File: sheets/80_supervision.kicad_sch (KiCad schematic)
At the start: 0 parts

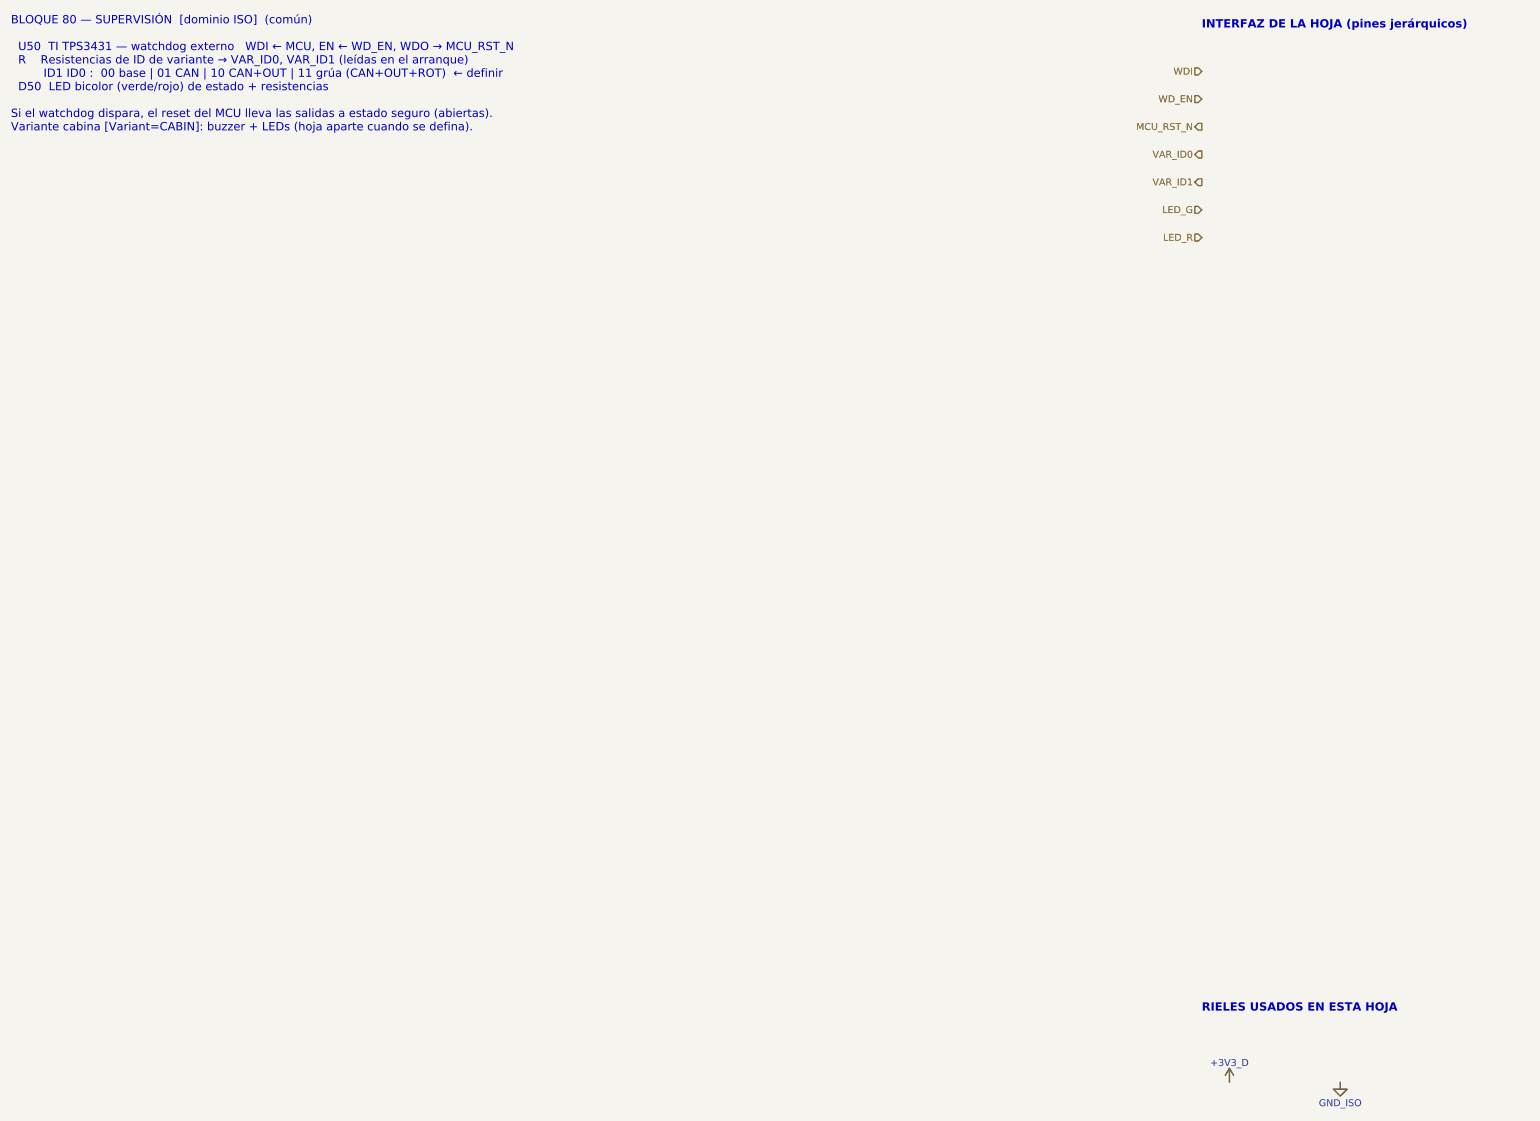
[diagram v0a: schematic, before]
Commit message: [Claude Code] 20_buck_5v: opción B (no aislada) con LMR38010; masas unificadas
- sheets/20_isolation -> sheets/20_buck_5v: se quitan PS201, ISO7763 y
  TPS7A1650; U201 LMR38010SQDDARQ1 (PROTO: LMR38010SDDAR, LCSC C5219310),
  5.02 V / 1 A a 400 kHz según TI SNVSC73B (L201 XAL6060-333, 3 x 22 uF,
  RT 64.9k, FB 100k/24.9k). Huella oficial HSOIC-8 con vías térmicas.
- Símbolo LMR38010 (easyeda2kicad) en lib/easyeda2kicad/INCLI-VA_easyeda,
  con tipos de pin ajustados; registrado en sym-lib-table.
- Todas las hojas: GND_ISO -> GND_VEH, +5V_ISO -> +5V_VEH.
- Raíz: EN/DIAG/FLT directos entre las hojas 40, 70 y 10; la hoja 20 sin pines.
- 10_power_input: R111 a +3V3_D, C109 = 100 nF (inrush con C105),
  C105 DNP solo en PROTO; se quita un PWR_FLAG suelto en GND_VEH.
- 70_output_ch: cambios de layout del usuario (hechos en KiCad).
- Textos de las hojas 30/40/50/80 y la raíz sin referencias al aislamiento.
- ERC: 0 en 10, 20, 30, 40, 50, 60 y 70; quedan los de 80 (hoja vacía).

Co-Authored-By: Claude Opus 5.5 <noreply@anthropic.com>
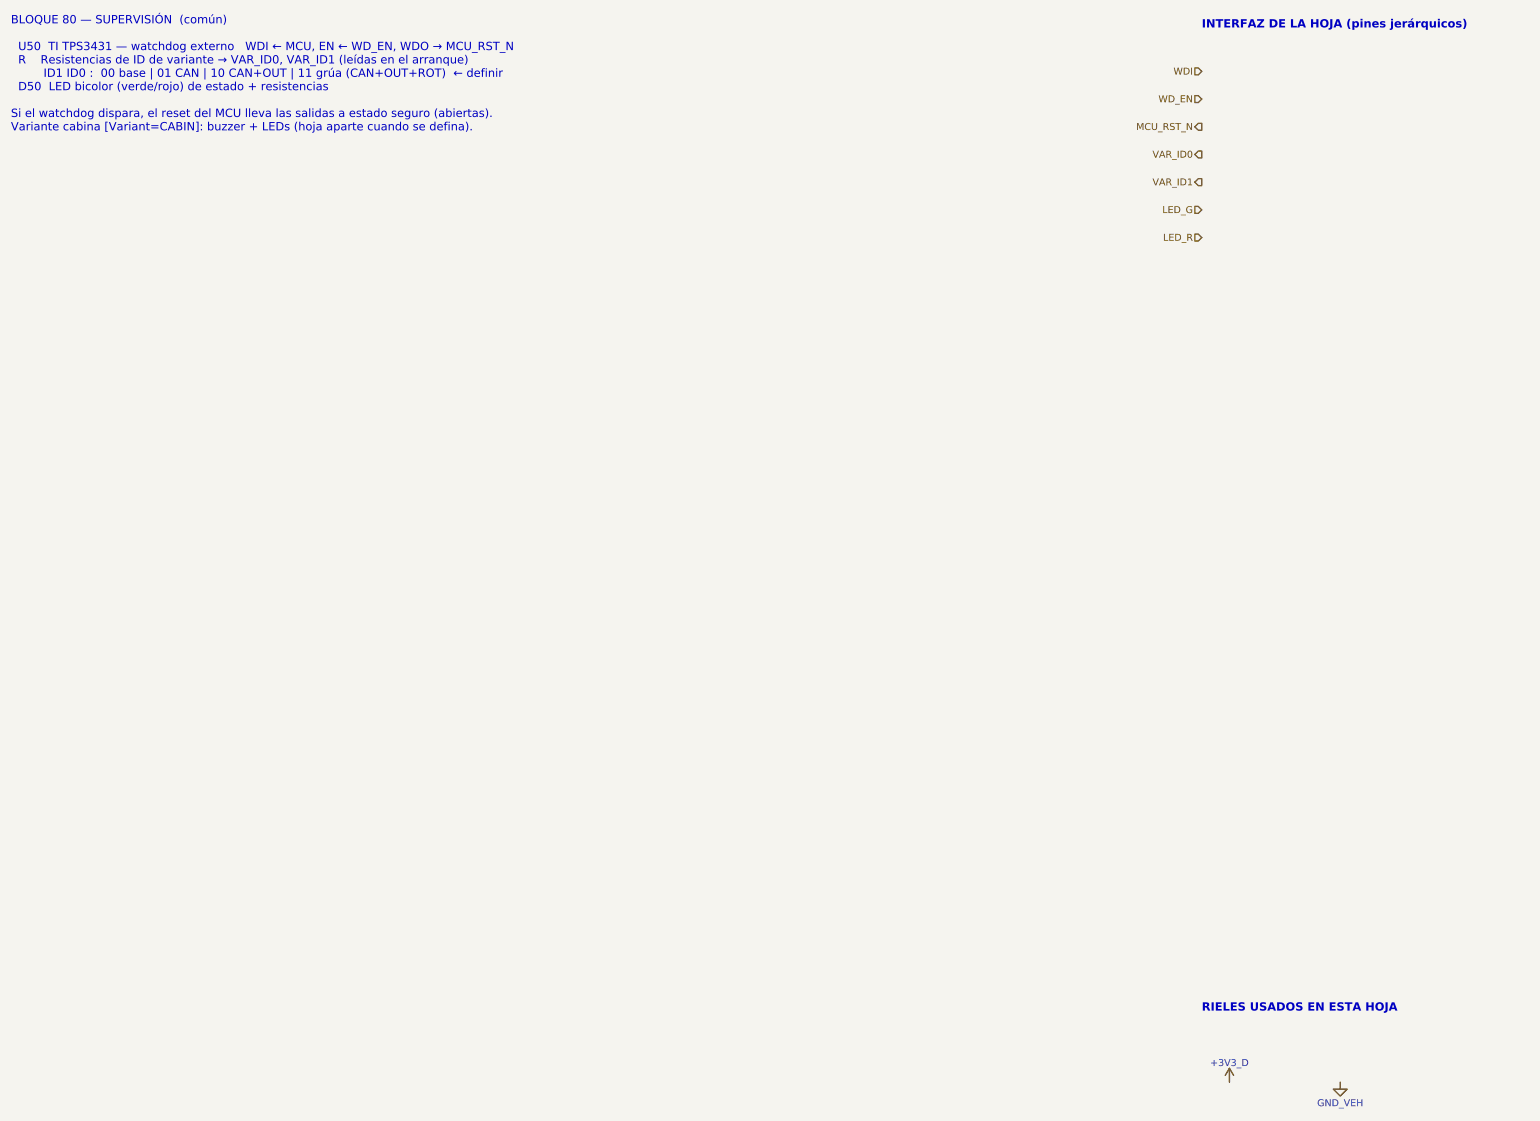
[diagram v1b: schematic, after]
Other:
- note added: "BLOQUE 80 — SUPERVISIÓN (común) U50 TI TPS3431 — watchdog externo WDI ← MCU, EN ← WD_EN, WDO → MCU_RST_N R Resistencias de ID de variante → VAR_ID0, VAR_ID1 (leídas en el arranque) ID1 ID0 : 00 base | 01 CAN | 10 CAN+OUT | 11 grúa (CAN+OUT+ROT) ← definir D50 LED bicolor (verde/rojo) de estado + resistencias Si el watchdog dispara, el reset del MCU lleva las salidas a estado seguro (abiertas). Var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"
- note removed: "BLOQUE 80 — SUPERVISIÓN [dominio ISO] (común) U50 TI TPS3431 — watchdog externo WDI ← MCU, EN ← WD_EN, WDO → MCU_RST_N R Resistencias de ID de variante → VAR_ID0, VAR_ID1 (leídas en el arranque) ID1 ID0 : 00 base | 01 CAN | 10 CAN+OUT | 11 grúa (CAN+OUT+ROT) ← definir D50 LED bicolor (verde/rojo) de estado + resistencias Si el watchdog dispara, el reset del MCU lleva las salidas a estado seguro (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"
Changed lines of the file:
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@@
 		(comment 2 "Inclinómetro de chasis CAN/BLE — INCLI-VA")
 	)
-	(text "BLOQUE 80 — SUPERVISIÓN  [dominio ISO]  (común)\n\n  U50  TI TPS3431 — watchdog externo   WDI ← MCU, EN ← WD_EN, WDO → MCU_RST_N\n  R    Resistencias de ID de variante → VAR_ID0, VAR_ID1 (leídas en el arranque)\n         ID1 ID0 :  00 base | 01 CAN | 10 CAN+OUT | 11 grúa (CAN+OUT+ROT)  ← definir\n  D50  LED bicolor (verde/rojo) de estado + resistencias\n\nSi el watchdog dispara, el reset del MCU lleva las salidas a estado seguro (abiertas).\nVariante cabina [Variant=CABIN]: buzzer + LEDs (hoja aparte cuando se defina)."
+	(text "BLOQUE 80 — SUPERVISIÓN  (común)\n\n  U50  TI TPS3431 — watchdog externo   WDI ← MCU, EN ← WD_EN, WDO → MCU_RST_N\n  R    Resistencias de ID de variante → VAR_ID0, VAR_ID1 (leídas en el arranque)\n         ID1 ID0 :  00 base | 01 CAN | 10 CAN+OUT | 11 grúa (CAN+OUT+ROT)  ← definir\n  D50  LED bicolor (verde/rojo) de estado + resistencias\n\nSi el watchdog dispara, el reset del MCU lleva las salidas a estado seguro (abiertas).\nVariante cabina [Variant=CABIN]: buzzer + LEDs (hoja aparte cuando se defina)."
 		(exclude_from_sim no)
 		(at 20.32 20.32 0)
@@
 	)
 	(symbol
-		(lib_id "INCLI-VA:GND_ISO")
+		(lib_id "INCLI-VA:GND_VEH")
 		(at 264.16 215.9 0)
 		(unit 1)
@@
 			)
 		)
-		(property "Value" "GND_ISO"
+		(property "Value" "GND_VEH"
 			(at 264.16 219.71 0)
 			(show_name no)

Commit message: [Claude Code] 80_supervision: TPS3828-33-Q1, LED y VAR_ID; J1/J2 verticales; contorno con muesca
- 80_supervision: U801 TPS3828-33QDBVRQ1 (supervisor de +3V3_D + watchdog,
  WDI <- IO17), R802 0 ohm, R801 DNP; LED verde/rojo DNP en PROD (caja
  opaca); VAR_ID0/1 (CAN/OUT) y VAR_ID2 (IO8, CABIN, DNP).
- WD_EN eliminado (IO18 libre); VAR_ID2 ocupa su pin en las hojas 40/80 y la raíz.
- 10_power_input: J1/J2 MSTBV 2,5 GF 5.08 verticales (1777109 / 1777073).
- lib: se borran los símbolos URB2405 y TPS7A1650; U101: vías del EP a Ø 0.45 mm.
- PCB: contorno único con muesca de 8 x 35 mm para la antena (antes, dos
  rectángulos superpuestos); serigrafía de U401 recortada en la muesca.
- ERC: 0 errores, 1 aviso intencional (U101_RTN).

Co-Authored-By: Claude Opus 5.5 <noreply@anthropic.com>
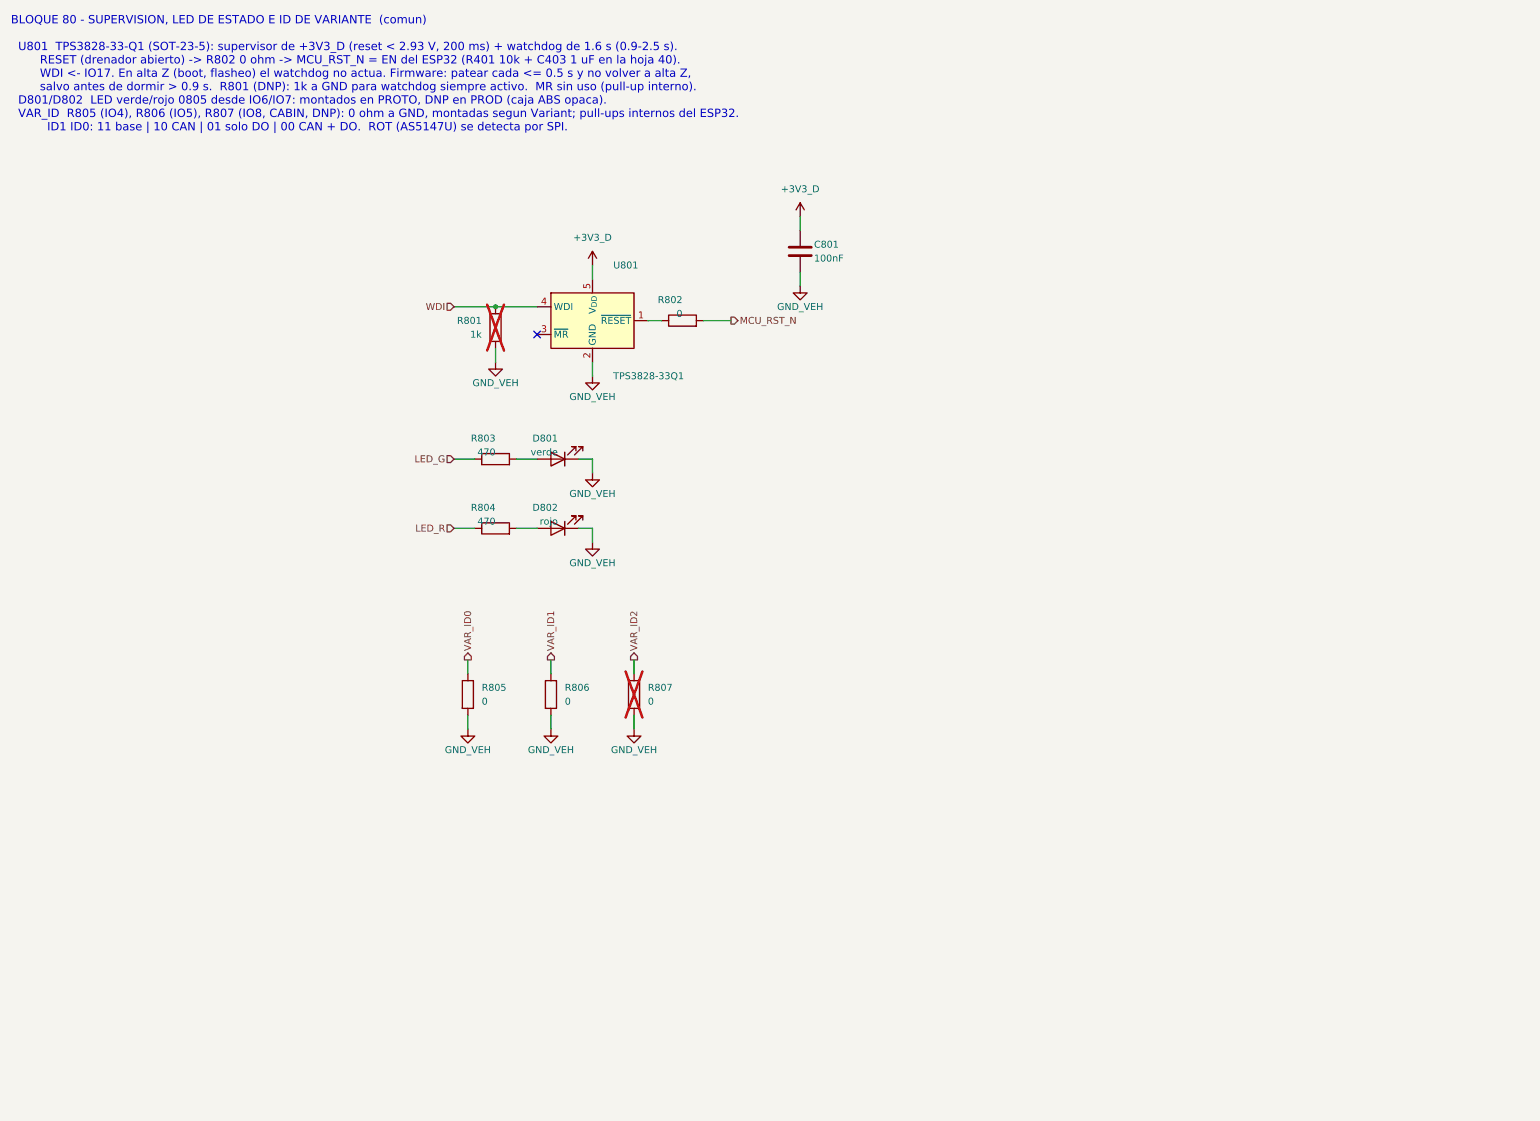
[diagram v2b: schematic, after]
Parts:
- added C801: 100nF, Capacitor_SMD:C_0603_1608Metric, symbol Device:C
- added D801: verde, LED_SMD:LED_0805_2012Metric, symbol Device:LED
- added D802: rojo, LED_SMD:LED_0805_2012Metric, symbol Device:LED
- added R801: 1k, Resistor_SMD:R_0603_1608Metric, symbol Device:R
- added R802, R805, R806, R807: 0, Resistor_SMD:R_0603_1608Metric, symbol Device:R
- added R803, R804: 470, Resistor_SMD:R_0603_1608Metric, symbol Device:R
- added U801: TPS3828-33Q1, Package_TO_SOT_SMD:SOT-23-5, symbol Power_Supervisor:TPS3823-xxDBV
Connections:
- net +3V3_D: now also C801.1, U801.5 (V_{DD})
- net GND_VEH: now also C801.2, D801.1 (K), D802.1 (K), R801.2, R805.2, R806.2, R807.2, U801.2 (GND)
- net LED_G: now also R803.1
- net LED_R: now also R804.1
- net MCU_RST_N: now also R802.2
- net VAR_ID0: now also R805.1
- net VAR_ID1: now also R806.1
- net WDI: now also R801.1, U801.4 (WDI)
- new net: D802.2 (A), R804.2
- new net: D801.2 (A), R803.2
- new net: R802.1, U801.1 (~{RESET})
- new net VAR_ID2: R807.1
- no-connect marks 0 -> 1
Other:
- note added: "BLOQUE 80 - SUPERVISION, LED DE ESTADO E ID DE VARIANTE (comun) U801 TPS3828-33-Q1 (SOT-23-5): supervisor de +3V3_D (reset < 2.93 V, 200 ms) + watchdog de 1.6 s (0.9-2.5 s). RESET (drenador abierto) -> R802 0 ohm -> MCU_RST_N = EN del ESP32 (R401 10k + C403 1 uF en la hoja 40). WDI <- IO17. En alta Z (boot, flasheo) el watchdog no actua. Firmware: patear cada <= 0.5 s y no volver a alta Z, salvo 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"
- note removed: "BLOQUE 80 — SUPERVISIÓN (común) U50 TI TPS3431 — watchdog externo WDI ← MCU, EN ← WD_EN, WDO → MCU_RST_N R Resistencias de ID de variante → VAR_ID0, VAR_ID1 (leídas en el arranque) ID1 ID0 : 00 base | 01 CAN | 10 CAN+OUT | 11 grúa (CAN+OUT+ROT) ← definir D50 LED bicolor (verde/rojo) de estado + resistencias Si el watchdog dispara, el reset del MCU lleva las salidas a estado seguro (abiertas). Var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"
- note removed: "INTERFAZ DE LA HOJA (pines jerárquicos)"
- note removed: "RIELES USADOS EN ESTA HOJA"
